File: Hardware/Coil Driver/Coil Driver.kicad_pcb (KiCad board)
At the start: 2 copper layers, 76 parts, among them J1 Barrel_Jack_Switch, J2 0.1" Header, J3 Tag-connect-NL, J4 0.1" Header, Q1 DMN3023L, Q2 DMN3023L, Q3 DMN3023L, Q4 DMN3023L, SW1 BTN_RST, SW2 BTN_USR1, SW3 BTN_USR2, U1 DGD05473, U2 MCP16331, U3 DGD05473, U4 STM32F070F6P6, Y1 8MHz

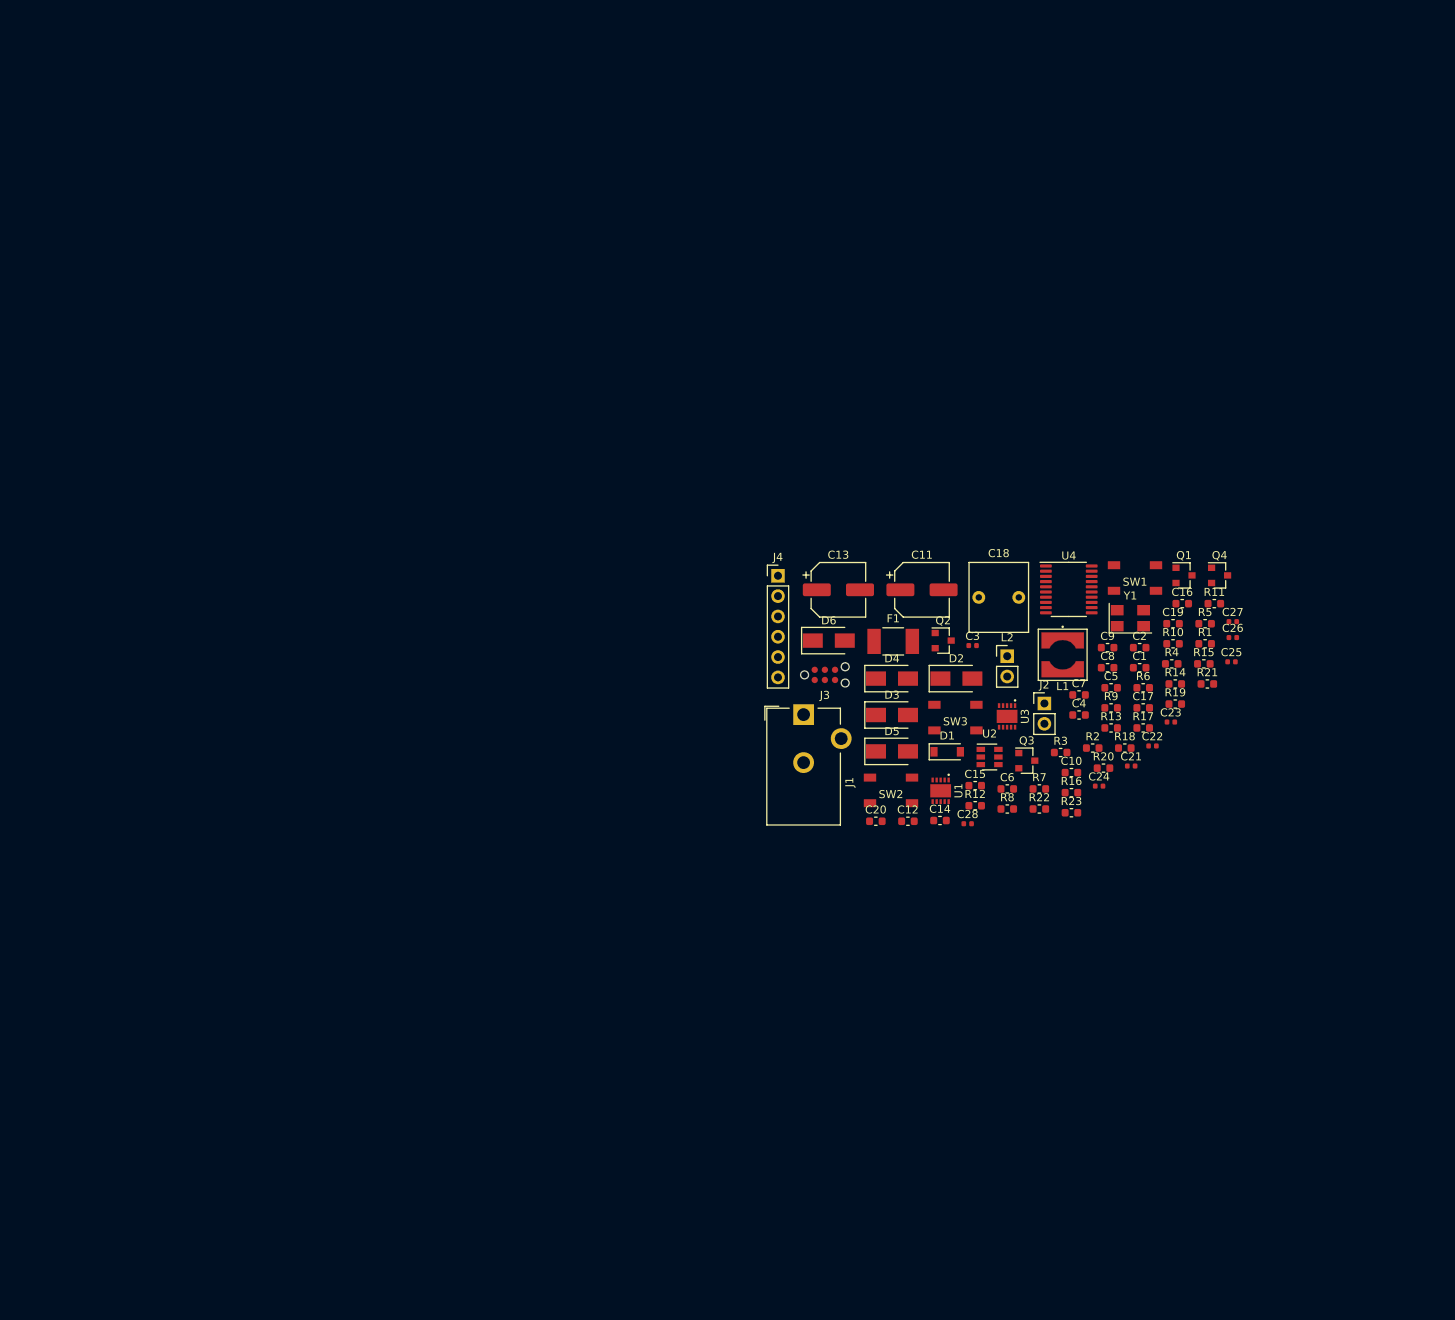
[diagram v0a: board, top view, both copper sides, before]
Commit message: imported footprints into PCB document. Added user LEDs and power indication LEDs to schematic.
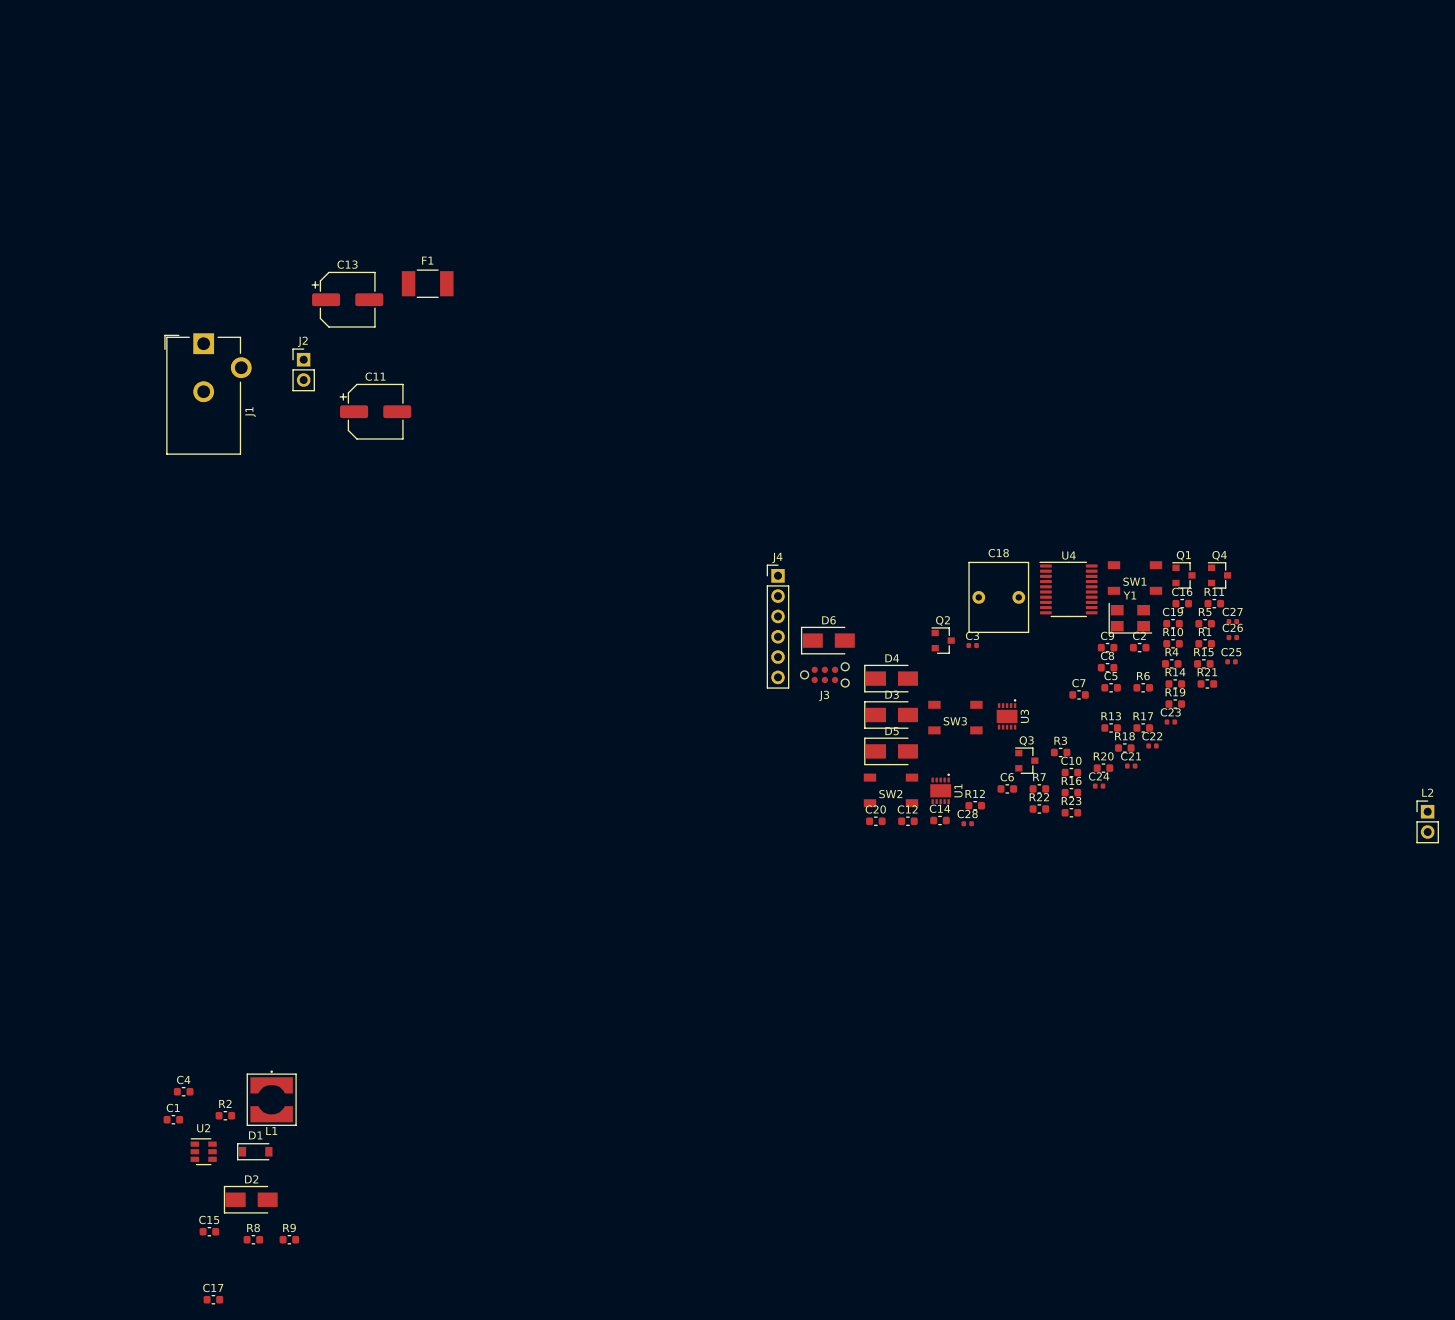
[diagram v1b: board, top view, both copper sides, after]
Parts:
- moved C17 137.8 mm to (33.7, 172.0)
- moved C1 133.3 mm to (28.7, 149.5)
- moved R9 122.4 mm to (43.2, 164.5)
- moved C4 121.4 mm to (30.0, 146.0)
- moved R2 117.8 mm to (35.2, 149.0)
- moved L1 113.4 mm to (41.0, 147.0)
- moved C15 110.8 mm to (33.2, 163.5)
- moved U2 109.9 mm to (32.5, 153.5)
- moved D2 109.6 mm to (38.5, 159.5)
- moved R8 108.5 mm to (38.7, 164.5)
- moved J2 102.1 mm to (45.0, 54.5)
- moved D1 99.9 mm to (39.0, 153.5)
- moved J1 88.2 mm to (32.5, 52.5)
- moved F1 73.4 mm to (60.5, 45.0)
- moved C11 71.8 mm to (54.0, 61.0)
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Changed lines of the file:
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@@
     (pad_to_mask_clearance 0.05)
     (aux_axis_origin 0 0)
-    (visible_elements FFFFFF7F)
+    (visible_elements FFFFF77F)
     (pcbplotparams
       (layerselection 0x010fc_ffffffff)
@@
   )
   (module Package_TO_SOT_SMD:SOT-23-6 (layer F.Cu)
-    (at 130.74 104.16)
+    (at 32.5 153.5)
     (descr "6-pin SOT-23 package")
     (tags SOT-23-6)
@@
   )
   (module Resistor_SMD:R_0603_1608Metric (layer F.Cu)
-    (at 145.93 98.02)
+    (at 43.2125 164.5)
     (descr "Resistor SMD 0603 (1608 Metric), square (rectangular) end terminal, IPC_7351 nominal, (Body size source: http://www.tortai-tech.com/upload/download/2011102023233369053.pdf), generated with kicad-footprint-generator")
     (tags resistor)
@@
   )
   (module Resistor_SMD:R_0603_1608Metric (layer F.Cu)
-    (at 132.95 110.66)
+    (at 38.7125 164.5)
     (descr "Resistor SMD 0603 (1608 Metric), square (rectangular) end terminal, IPC_7351 nominal, (Body size source: http://www.tortai-tech.com/upload/download/2011102023233369053.pdf), generated with kicad-footprint-generator")
     (tags resistor)
@@
   )
   (module Resistor_SMD:R_0603_1608Metric (layer F.Cu)
-    (at 143.63 103.04)
+    (at 35.2125 149)
     (descr "Resistor SMD 0603 (1608 Metric), square (rectangular) end terminal, IPC_7351 nominal, (Body size source: http://www.tortai-tech.com/upload/download/2011102023233369053.pdf), generated with kicad-footprint-generator")
     (tags resistor)
@@
   )
   (module Connector_PinHeader_2.54mm:PinHeader_1x02_P2.54mm_Vertical (layer F.Cu)
-    (at 132.94 91.56)
+    (at 185.5 111)
     (descr "Through hole straight pin header, 1x02, 2.54mm pitch, single row")
     (tags "Through hole pin header THT 1x02 2.54mm single row")
@@
   )
   (module MyParts:744042150 (layer F.Cu)
-    (at 139.875 91.385)
+    (at 41 147)
     (fp_text reference L1 (at 0 3.95) (layer F.SilkS)
       (effects (font (size 1 1) (thickness 0.15)))
@@
   )
   (module Connector_PinHeader_2.54mm:PinHeader_1x02_P2.54mm_Vertical (layer F.Cu)
-    (at 137.59 97.47)
+    (at 45 54.5)
     (descr "Through hole straight pin header, 1x02, 2.54mm pitch, single row")
     (tags "Through hole pin header THT 1x02 2.54mm single row")
@@
   )
   (module Connector_BarrelJack:BarrelJack_CUI_PJ-102AH_Horizontal (layer F.Cu)
-    (at 107.49 98.86)
+    (at 32.5 52.5)
     (descr "Thin-pin DC Barrel Jack, https://cdn-shop.adafruit.com/datasheets/21mmdcjackDatasheet.pdf")
     (tags "Power Jack")
@@
   )
   (module MyParts:miniSMDC110F_16-2 (layer F.Cu)
-    (at 118.69 89.71)
+    (at 60.5 45)
     (descr "Littelfuse miniSMDC110F/16-2 resettable fuse")
     (tags "Littelfuse resettable fuse")
@@
   )
   (module Diode_SMD:D_SMA (layer F.Cu)
-    (at 126.59 94.36)
+    (at 38.5 159.5)
     (descr "Diode SMA (DO-214AC)")
     (tags "Diode SMA (DO-214AC)")
@@
   )
   (module Diode_SMD:D_SOD-123 (layer F.Cu)
-    (at 125.44 103.51)
+    (at 39 153.5)
     (descr SOD-123)
     (tags SOD-123)
@@
   )
   (module Capacitor_SMD:C_0603_1608Metric (layer F.Cu)
-    (at 149.94 98.02)
+    (at 33.7125 172)
     (descr "Capacitor SMD 0603 (1608 Metric), square (rectangular) end terminal, IPC_7351 nominal, (Body size source: http://www.tortai-tech.com/upload/download/2011102023233369053.pdf), generated with kicad-footprint-generator")
     (tags capacitor)
@@
   )
   (module Capacitor_SMD:C_0603_1608Metric (layer F.Cu)
-    (at 128.94 107.74)
+    (at 33.2125 163.5)
     (descr "Capacitor SMD 0603 (1608 Metric), square (rectangular) end terminal, IPC_7351 nominal, (Body size source: http://www.tortai-tech.com/upload/download/2011102023233369053.pdf), generated with kicad-footprint-generator")
     (tags capacitor)
@@
   )
   (module Capacitor_SMD:CP_Elec_6.3x7.7 (layer F.Cu)
-    (at 111.84 83.26)
+    (at 50.5 47)
     (descr "SMD capacitor, aluminum electrolytic, Nichicon, 6.3x7.7mm")
     (tags "capacitor electrolytic")
@@
   )
   (module Capacitor_SMD:CP_Elec_6.3x7.7 (layer F.Cu)
-    (at 122.29 83.26)
+    (at 54 61)
     (descr "SMD capacitor, aluminum electrolytic, Nichicon, 6.3x7.7mm")
     (tags "capacitor electrolytic")
@@
   )
   (module Capacitor_SMD:C_0603_1608Metric (layer F.Cu)
-    (at 141.92 98.91)
+    (at 30 146)
     (descr "Capacitor SMD 0603 (1608 Metric), square (rectangular) end terminal, IPC_7351 nominal, (Body size source: http://www.tortai-tech.com/upload/download/2011102023233369053.pdf), generated with kicad-footprint-generator")
     (tags capacitor)
@@
   )
   (module Capacitor_SMD:C_0603_1608Metric (layer F.Cu)
-    (at 149.5 93)
+    (at 28.7125 149.5)
     (descr "Capacitor SMD 0603 (1608 Metric), square (rectangular) end terminal, IPC_7351 nominal, (Body size source: http://www.tortai-tech.com/upload/download/2011102023233369053.pdf), generated with kicad-footprint-generator")
     (tags capacitor)

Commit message: Swapped out 8MHz crystal for 2 pin instead of 4 pin. Initial part placement (except for gate drivers/h-bridge) loosely complete. Decided board will be 4 layers to make routing of power nets easier.
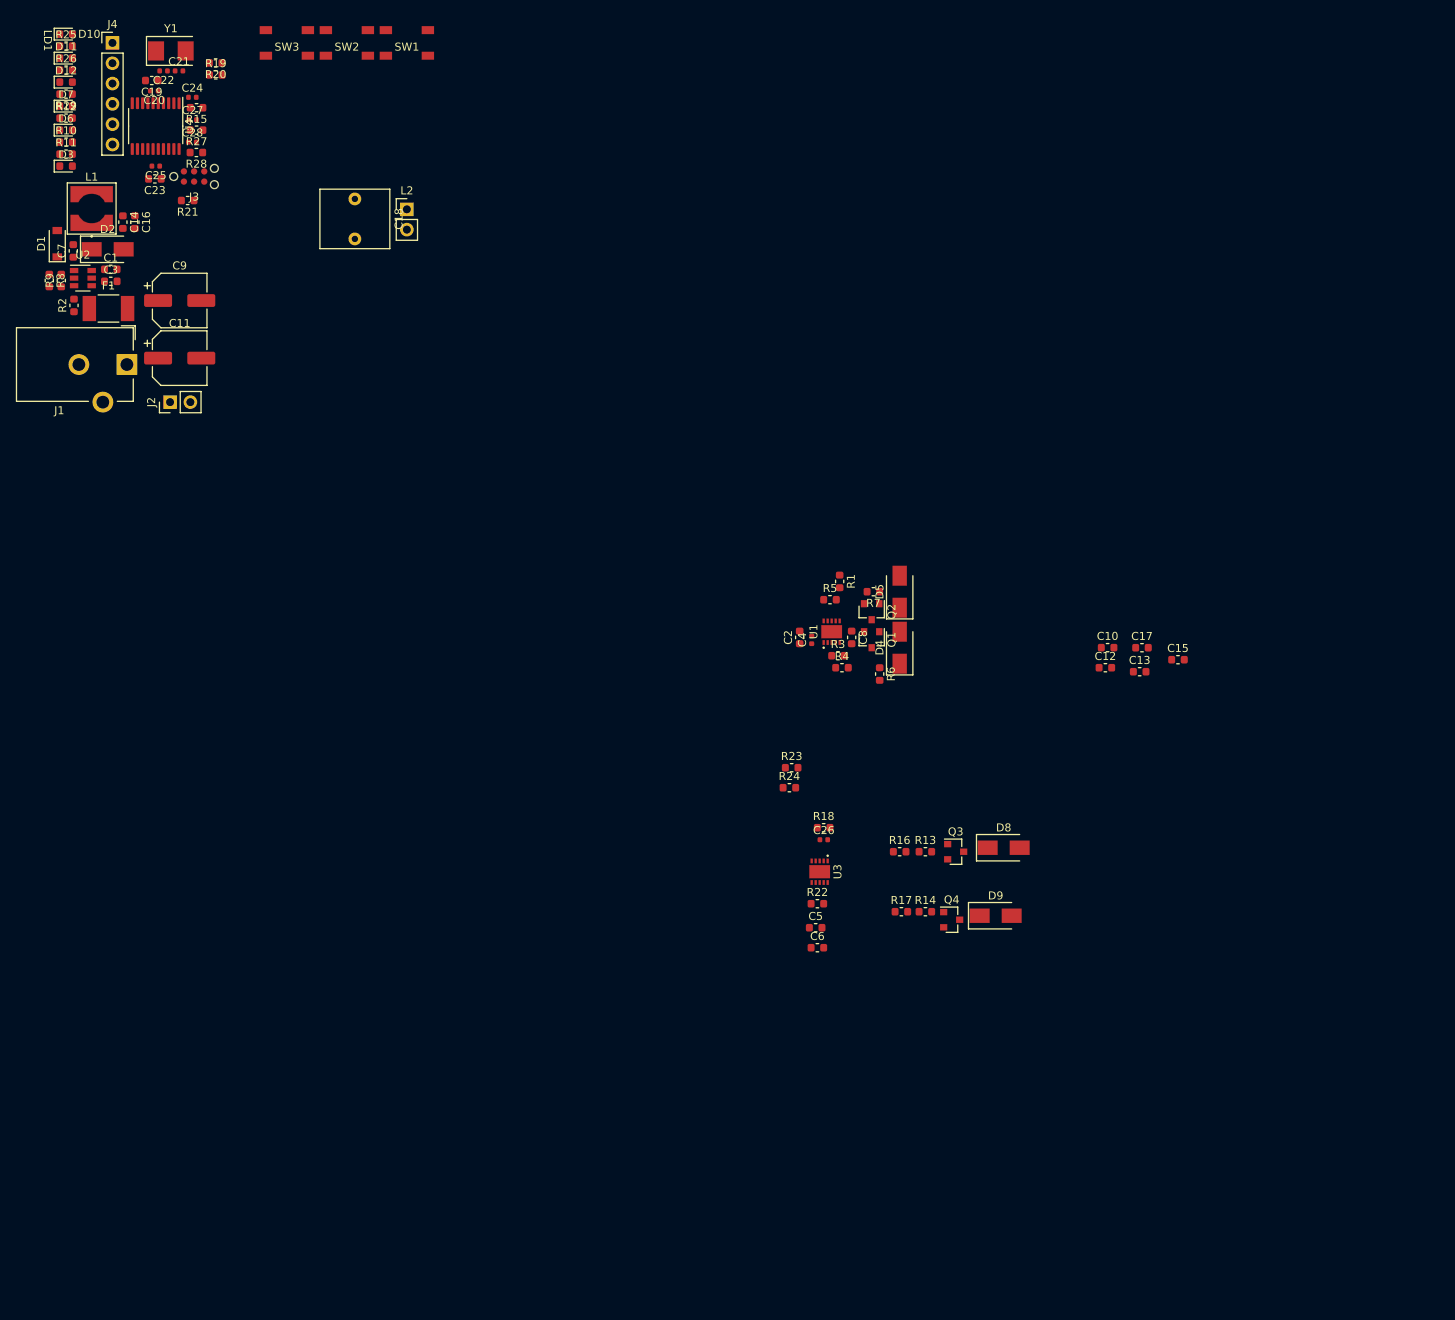
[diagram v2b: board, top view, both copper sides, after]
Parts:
- removed the C12 at (120.5, 112.2)
- removed the C17 at (33.7, 172.0)
- removed the R16 at (141.0, 108.6)
- removed the R17 at (149.9, 100.5)
- removed the R18 at (147.6, 103.0)
- removed the R22 at (137.0, 110.7)
- added C13: 10uF, Capacitor_SMD:C_0603_1608Metric, F.Cu at (149.5, 93.5)
- added C16: 10uF, Capacitor_SMD:C_0603_1608Metric, F.Cu at (23.9, 37.3)
- added D10: GRN, LED_SMD:LED_0603_1608Metric, F.Cu at (15.3, 13.8)
- added D11: GRN, LED_SMD:LED_0603_1608Metric, F.Cu at (15.3, 16.8)
- added D12: GRN, LED_SMD:LED_0603_1608Metric, F.Cu at (15.3, 19.8)
- added D5: B2100A, Diode_SMD:D_SMA, F.Cu at (119.5, 83.5)
- added D6: GRN, LED_SMD:LED_0603_1608Metric, F.Cu at (15.3, 25.8)
- added D7: GRN, LED_SMD:LED_0603_1608Metric, F.Cu at (15.3, 22.8)
- added R10: 4.7k, Resistor_SMD:R_0603_1608Metric, F.Cu at (15.3, 27.3)
- added R11: 4.7k, Resistor_SMD:R_0603_1608Metric, F.Cu at (15.3, 28.8)
- added R15: 10k, Resistor_SMD:R_0603_1608Metric, F.Cu at (31.6, 23.0)
- added R19: 10k, Resistor_SMD:R_0603_1608Metric, F.Cu at (34.0, 18.9)
- added R20: 10k, Resistor_SMD:R_0603_1608Metric, F.Cu at (34.0, 17.4)
- added R21: 0, Resistor_SMD:R_0603_1608Metric, F.Cu at (30.5, 34.6)
- added R25: 680, Resistor_SMD:R_0603_1608Metric, F.Cu at (15.3, 15.3)
- added R26: 680, Resistor_SMD:R_0603_1608Metric, F.Cu at (15.3, 18.3)
- added R27: 10k, Resistor_SMD:R_0603_1608Metric, F.Cu at (31.6, 25.8)
- added R29: 680, Resistor_SMD:R_0603_1608Metric, F.Cu at (15.3, 21.3)
- C20: value 4.7uF -> 10nF; footprint Capacitor_SMD:C_0603_1608Metric -> Capacitor_SMD:C_0402_1005Metric
- C21: value 10nF -> 20pF
- C22: value 100nF -> 20pF
- C23: value 20pF -> 4.7uF; footprint Capacitor_SMD:C_0402_1005Metric -> Capacitor_SMD:C_0603_1608Metric
- C24: value 20pF -> 100nF
- C3: value 100nF -> 10uF; footprint Capacitor_SMD:C_0402_1005Metric -> Capacitor_SMD:C_0603_1608Metric
- C4: value 10uF -> 100nF; footprint Capacitor_SMD:C_0603_1608Metric -> Capacitor_SMD:C_0402_1005Metric
- D3: value B2100A -> GRN; footprint Diode_SMD:D_SMA -> LED_SMD:LED_0603_1608Metric
- R12: value 10k -> 680
- Y1: footprint Crystal:Crystal_SMD_5032-4Pin_5.0x3.2mm -> Crystal:Crystal_SMD_5032-2Pin_5.0x3.2mm
- moved C22 149.7 mm to (27.5, 18.4), turned to 180 degrees
- moved L2 148.2 mm to (57.9, 35.7)
- moved C25 148.1 mm to (26.5, 30.3), turned to 180 degrees
- moved C21 147.4 mm to (29.4, 18.4)
- moved C19 144.6 mm to (26.0, 19.6), turned to 180 degrees
- moved C27 144.4 mm to (31.1, 24.5)
- moved C23 144.0 mm to (26.4, 31.9), turned to 180 degrees
- moved R12 142.5 mm to (15.3, 24.3)
- moved C24 142.3 mm to (31.1, 21.7)
- moved C15 140.6 mm to (154.3, 92.0)
- moved Y1 139.3 mm to (28.4, 15.9)
- moved C7 137.4 mm to (16.2, 40.9), turned to 90 degrees
- moved R28 137.0 mm to (31.6, 28.6), turned to 180 degrees
- moved C28 129.0 mm to (31.1, 27.3)
- moved C20 128.3 mm to (26.3, 20.9), turned to 180 degrees
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- renumbered C9 to C10, C13 to C11, C10 to C12, C16 to C17, C11 to C9, D5 to D8, D6 to D9, R10 to R13, R11 to R14, R13 to R16, R14 to R17, R15 to R18, R19 to R22, R20 to R23, R21 to R24, R23 to R28
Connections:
- net Net-(J4-Pad1) renamed /LD1
- net Net-(J4-Pad2) renamed /LD2
- net Net-(J4-Pad3) renamed /LD3
- C14 pad 1: +12V -> +3V3
- C15 pad 1: +3V3 -> +12V
- C21 pad 1: +3V3 -> Net-(C21-Pad1)
- C22 pad 1: +3V3 -> Net-(C22-Pad1)
- C23 pad 1: Net-(C23-Pad1) -> +3V3
- C25 pad 1: Net-(C25-Pad1) -> +3V3
- C7 pad 1: /VSW+ -> Net-(C7-Pad1)
- C8 pad 1: Net-(C8-Pad1) -> /VSW+
- D1 pad 1: Net-(C8-Pad1) -> Net-(C7-Pad1)
- D2 pad 1: Net-(C8-Pad2) -> Net-(C7-Pad2)
- D3 pad 1: +12V -> Net-(D3-Pad1)
- D3 pad 2: /VSW+ -> +12V
- D4 pad 1: /VSW+ -> +12V
- D4 pad 2: GND -> /VSW+
- L1 pad 1: Net-(C8-Pad2) -> Net-(C7-Pad2)
- R12 pad 1: +3V3 -> Net-(D7-Pad1)
- R12 pad 2: Net-(C25-Pad1) -> GND
- R3 pad 2: Net-(C7-Pad2) -> Net-(C8-Pad2)
- SW1 pad 2: Net-(C25-Pad1) -> Net-(C24-Pad1)
- U2 pad 1: Net-(C8-Pad1) -> Net-(C7-Pad1)
- U2 pad 6: Net-(C8-Pad2) -> Net-(C7-Pad2)
- U4 pad 2: Net-(C23-Pad1) -> Net-(C21-Pad1)
- U4 pad 3: Net-(C24-Pad1) -> Net-(C22-Pad1)
- U4 pad 4: Net-(C25-Pad1) -> Net-(C24-Pad1)
- Y1 pad 1: Net-(C23-Pad1) -> Net-(C22-Pad1)
- Y1 pad 2: GND -> Net-(C21-Pad1)
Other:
- board text added: "LD1"
